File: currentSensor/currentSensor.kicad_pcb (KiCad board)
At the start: 2 copper layers, 60 x 100 mm, 54 parts, among them J1 Conn_01x09_Male, J2 Conn_01x09_Male, J3 Screw_Terminal_01x08, J4 Screw_Terminal_01x02, J5 Screw_Terminal_01x08, U1 PC847, U2 PC847, U3 PC847, U4 PC847

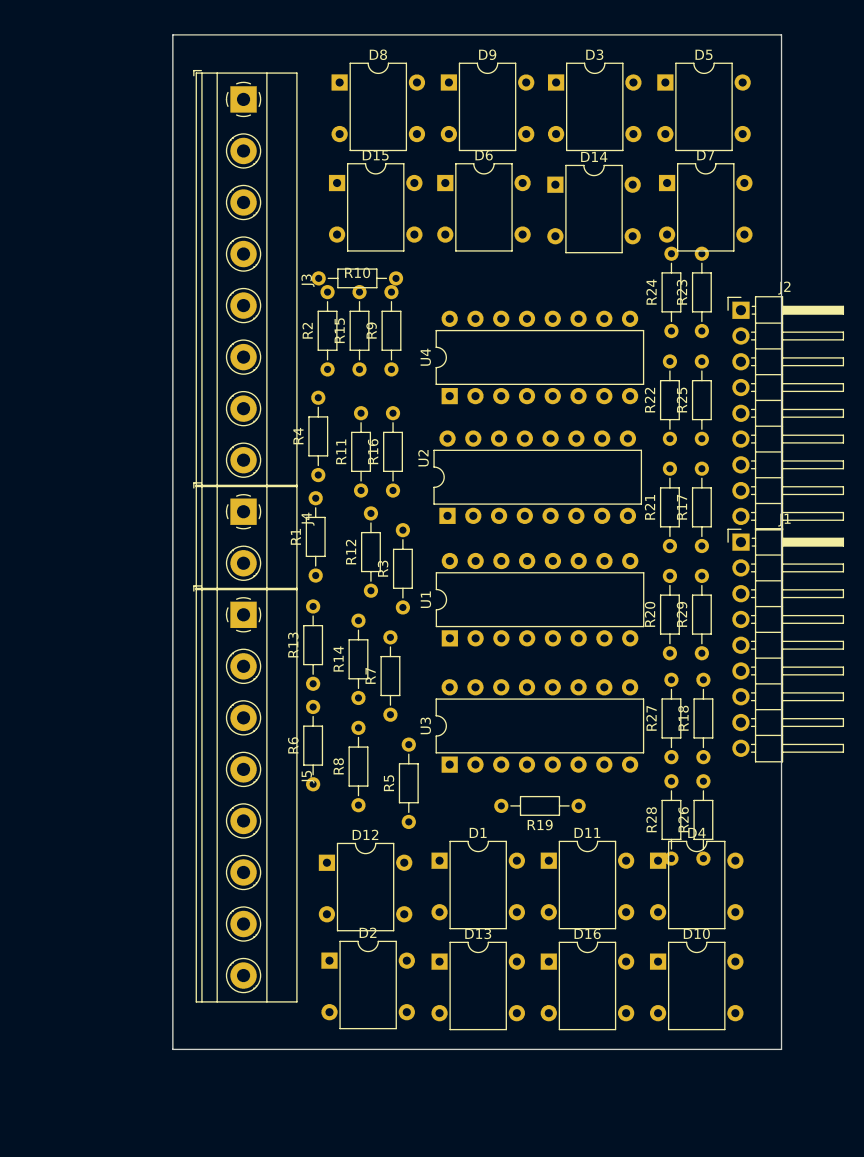
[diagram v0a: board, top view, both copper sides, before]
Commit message: added some changed to the current sensor. There also seems a bug with the mcp23017. I suspect the chip itself may be damaged. Not all pins are at 5V
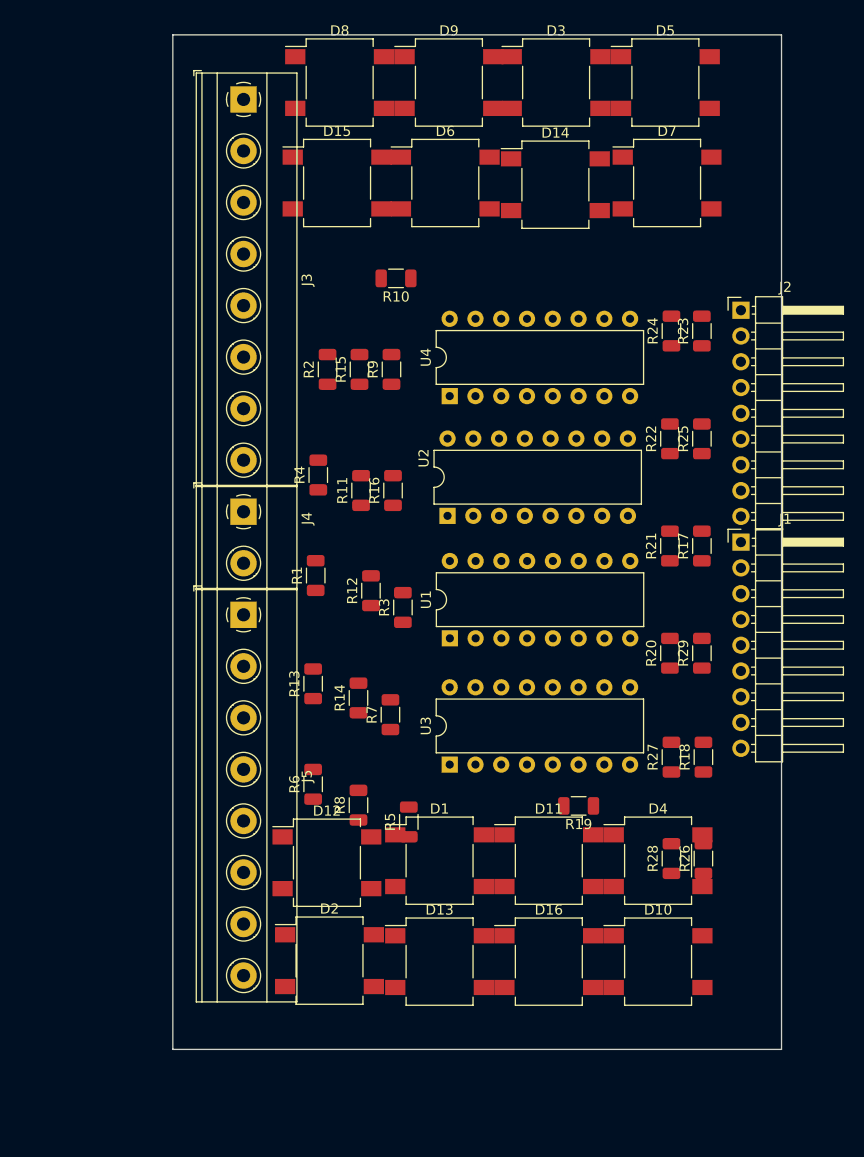
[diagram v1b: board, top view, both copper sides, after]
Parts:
- D1, D10, D11, D12, D13, D14, D15, D16, D2, D3, D4, D5, D6, D7, D8, D9: footprint Diode_THT:Diode_Bridge_DIP-4_W7.62mm_P5.08mm -> Diode_SMD:Diode_Bridge_Diotec_SO-DIL-Slim
- R1, R10, R11, R12, R13, R14, R15, R16, R17, R18, R19, R2, R20, R21, R22, R23, R24, R25, R26, R27, R28, R29, R3, R4, R5, R6, R7, R8, R9: footprint Resistor_THT:R_Axial_DIN0204_L3.6mm_D1.6mm_P7.62mm_Horizontal -> Resistor_SMD:R_1206_3216Metric

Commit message: added separate HAL files for NX and empty files for the MCP23017. They need filling in for read and write registers
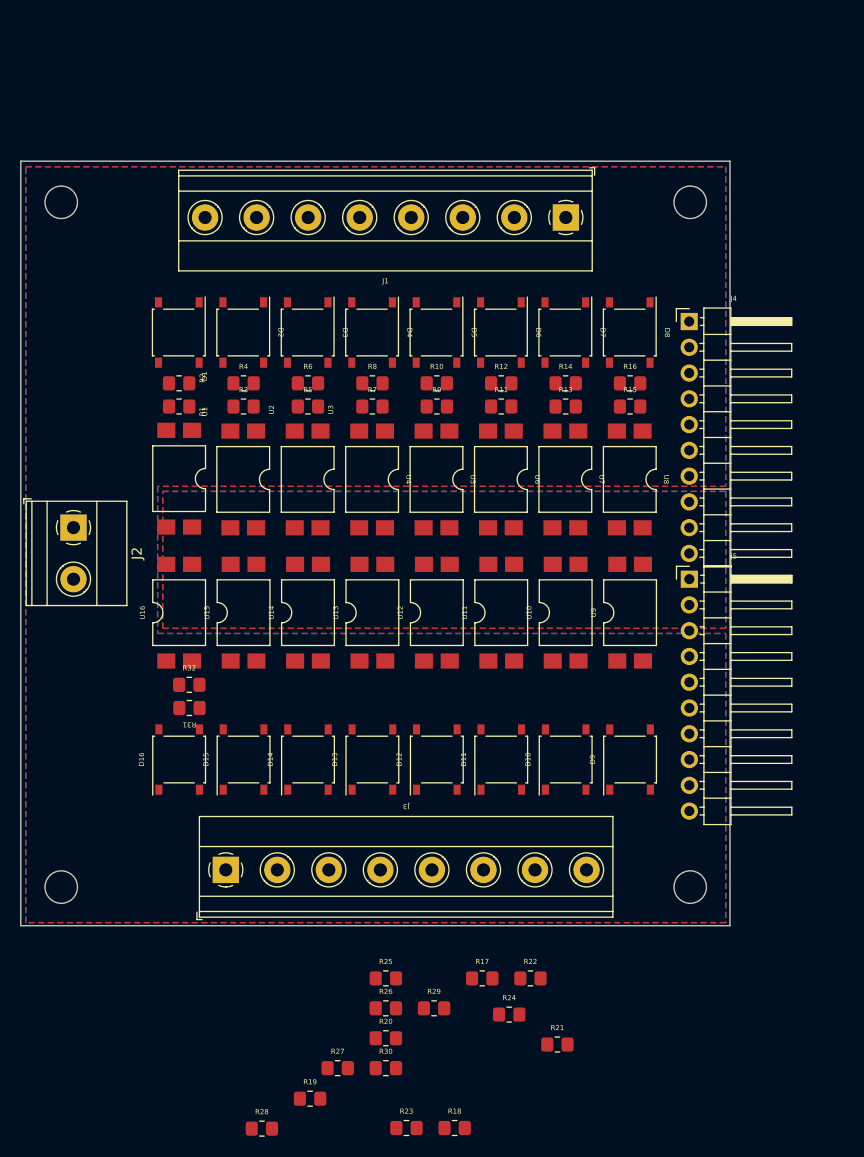
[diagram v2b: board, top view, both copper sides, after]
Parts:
- added R30: 4k7, Resistor_SMD:R_0805_2012Metric_Pad1.20x1.40mm_HandSolder, F.Cu at (44.0, 152.8)
- added R31: 47R, Resistor_SMD:R_0805_2012Metric_Pad1.20x1.40mm_HandSolder, F.Cu at (24.6, 117.3)
- added R32: 4k7, Resistor_SMD:R_0805_2012Metric_Pad1.20x1.40mm_HandSolder, F.Cu at (24.6, 115.1)
- added REF**: MountingHole_3.2mm_M3, MountingHole:MountingHole_3.2mm_M3, F.Cu at (74.0, 67.5)
- added REF**: MountingHole_3.2mm_M3, MountingHole:MountingHole_3.2mm_M3, F.Cu at (74.0, 135.0)
- added REF**: MountingHole_3.2mm_M3, MountingHole:MountingHole_3.2mm_M3, F.Cu at (12.0, 67.5)
- added REF**: MountingHole_3.2mm_M3, MountingHole:MountingHole_3.2mm_M3, F.Cu at (12.0, 135.0)
- added U10: SFH6206-2T, Package_DIP:SMDIP-4_W9.53mm_Clearance8mm, F.Cu at (61.7, 108.0)
- added U11: SFH6206-2T, Package_DIP:SMDIP-4_W9.53mm_Clearance8mm, F.Cu at (55.4, 108.0)
- added U12: SFH6206-2T, Package_DIP:SMDIP-4_W9.53mm_Clearance8mm, F.Cu at (49.0, 108.0)
- added U13: SFH6206-2T, Package_DIP:SMDIP-4_W9.53mm_Clearance8mm, F.Cu at (42.7, 108.0)
- added U14: SFH6206-2T, Package_DIP:SMDIP-4_W9.53mm_Clearance8mm, F.Cu at (36.3, 108.0)
- added U15: SFH6206-2T, Package_DIP:SMDIP-4_W9.53mm_Clearance8mm, F.Cu at (30.0, 108.0)
- added U16: SFH6206-2T, Package_DIP:SMDIP-4_W9.53mm_Clearance8mm, F.Cu at (23.6, 108.0)
- added U5: SFH6206-2T, Package_DIP:SMDIP-4_W9.53mm_Clearance8mm, F.Cu at (49.0, 94.8)
- added U6: SFH6206-2T, Package_DIP:SMDIP-4_W9.53mm_Clearance8mm, F.Cu at (55.3, 94.8)
- added U7: SFH6206-2T, Package_DIP:SMDIP-4_W9.53mm_Clearance8mm, F.Cu at (61.7, 94.8)
- added U8: SFH6206-2T, Package_DIP:SMDIP-4_W9.53mm_Clearance8mm, F.Cu at (68.0, 94.8)
- added U9: SFH6206-2T, Package_DIP:SMDIP-4_W9.53mm_Clearance8mm, F.Cu at (68.1, 108.0)
- D1, D10, D11, D12, D13, D14, D15, D16, D2, D3, D4, D5, D6, D7, D8, D9: value D -> ABS2; footprint Diode_SMD:Diode_Bridge_Diotec_SO-DIL-Slim -> Diode_SMD:Diode_Bridge_Diotec_ABS
- J1: value Conn_01x09_Male -> Screw_Terminal_01x08; footprint Connector_PinHeader_2.54mm:PinHeader_1x09_P2.54mm_Horizontal -> TerminalBlock_Phoenix:TerminalBlock_Phoenix_MKDS-1,5-8-5.08_1x08_P5.08mm_Horizontal
- J2: value Conn_01x09_Male -> Screw_Terminal_01x02; footprint Connector_PinHeader_2.54mm:PinHeader_1x09_P2.54mm_Horizontal -> TerminalBlock_Phoenix:TerminalBlock_Phoenix_MKDS-1,5-2-5.08_1x02_P5.08mm_Horizontal
- J4: value Screw_Terminal_01x02 -> Conn_01x10_Male; footprint TerminalBlock_Phoenix:TerminalBlock_Phoenix_MKDS-1,5-2-5.08_1x02_P5.08mm_Horizontal -> Connector_PinHeader_2.54mm:PinHeader_1x10_P2.54mm_Horizontal
- J5: value Screw_Terminal_01x08 -> Conn_01x10_Male; footprint TerminalBlock_Phoenix:TerminalBlock_Phoenix_MKDS-1,5-8-5.08_1x08_P5.08mm_Horizontal -> Connector_PinHeader_2.54mm:PinHeader_1x10_P2.54mm_Horizontal
- R1, R11, R13, R15, R17, R19, R21, R23, R25, R27, R29, R3, R5, R7, R9: value R -> 47R; footprint Resistor_SMD:R_1206_3216Metric -> Resistor_SMD:R_0805_2012Metric_Pad1.20x1.40mm_HandSolder
- R10, R12, R14, R16, R18, R2, R20, R22, R24, R26, R28, R4, R6, R8: value R -> 4k7; footprint Resistor_SMD:R_1206_3216Metric -> Resistor_SMD:R_0805_2012Metric_Pad1.20x1.40mm_HandSolder
- U1, U2, U3, U4: value PC847 -> SFH6206-2T; footprint Package_DIP:DIP-16_W7.62mm -> Package_DIP:SMDIP-4_W9.53mm_Clearance8mm
- moved R23 83.8 mm to (46.0, 158.8), turned to 0 degrees
- moved J3 76.0 mm to (28.2, 133.3), turned to 0 degrees
- moved R24 69.2 mm to (56.2, 147.6), turned to 0 degrees
- moved J2 69.2 mm to (13.2, 99.6), turned to -90 degrees
- moved D9 69.1 mm to (68.1, 122.4), turned to 90 degrees
- moved D2 62.5 mm to (29.9, 80.3), turned to -90 degrees
- moved D14 61.7 mm to (36.3, 122.4), turned to 90 degrees
- moved R25 61.6 mm to (44.0, 144.0), turned to 0 degrees
- moved D4 59.2 mm to (42.6, 80.3), turned to -90 degrees
- moved D1 58.1 mm to (23.6, 80.3), turned to -90 degrees
- moved D15 57.6 mm to (30.0, 122.4), turned to 90 degrees
- moved R22 54.9 mm to (58.2, 144.0), turned to 0 degrees
- moved R21 50.4 mm to (60.9, 150.5), turned to 0 degrees
- moved R28 48.4 mm to (31.8, 158.8), turned to 0 degrees
- moved R17 47.8 mm to (53.5, 144.0), turned to 0 degrees
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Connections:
- D1 pad 3: track5 -> track1
- D2 pad 3: track6 -> track2
- D3 pad 3: track7 -> track3
- D4 pad 3: track8 -> track4
- D5 pad 3: track1 -> track5
- D6 pad 3: track2 -> track6
- D7 pad 3: track3 -> track7
- D8 pad 3: track4 -> track8
- J1 pad 1: GND -> track8
- J1 pad 2: inp8 -> track7
- J1 pad 3: inp7 -> track6
- J1 pad 4: inp6 -> track5
- J1 pad 5: inp5 -> track4
- J1 pad 6: inp4 -> track3
- J1 pad 7: inp3 -> track2
- J1 pad 8: inp2 -> track1
- J2 pad 1: inp16 -> COM
- J2 pad 2: inp15 -> COM
- J3 pad 1: track1 -> track16
- J3 pad 2: track2 -> track15
- J3 pad 3: track3 -> track14
- J3 pad 4: track4 -> track13
- J3 pad 5: track5 -> track12
- J3 pad 6: track6 -> track11
- J3 pad 7: track7 -> track10
- J3 pad 8: track8 -> track9
- J4 pad 1: COM -> +5V
- J4 pad 2: COM -> inp1
- J5 pad 1: track9 -> +5V
- J5 pad 2: track10 -> inp9
- J5 pad 3: track11 -> inp10
- J5 pad 4: track12 -> inp11
- J5 pad 5: track13 -> inp12
- J5 pad 6: track14 -> inp13
- J5 pad 7: track15 -> inp14
- J5 pad 8: track16 -> inp15
- R1 pad 1: track5 -> track1
- R10 pad 1: track10 -> track5
- R10 pad 2: Net-(R10-Pad2) -> COM
- R11 pad 1: track11 -> track6
- R12 pad 1: track12 -> track6
- R12 pad 2: Net-(R12-Pad2) -> COM
- R13 pad 1: track13 -> track7
- R14 pad 1: track14 -> track7
- R14 pad 2: Net-(R14-Pad2) -> COM
- R15 pad 1: track15 -> track8
- R16 pad 1: track16 -> track8
- R16 pad 2: Net-(R16-Pad2) -> COM
- R17 pad 1: track5 -> track9
- R17 pad 2: COM -> Net-(R17-Pad2)
- R18 pad 1: track6 -> track9
- R19 pad 1: track7 -> track10
- R19 pad 2: COM -> Net-(R19-Pad2)
- R2 pad 1: track6 -> track1
- R2 pad 2: Net-(R2-Pad2) -> COM
- R20 pad 1: track8 -> track10
- R21 pad 1: track1 -> track11
- R21 pad 2: COM -> Net-(R21-Pad2)
- R22 pad 1: track2 -> track11
- R23 pad 1: track3 -> track12
- R23 pad 2: COM -> Net-(R23-Pad2)
- R24 pad 1: track4 -> track12
- R25 pad 1: track9 -> track13
- R25 pad 2: COM -> Net-(R25-Pad2)
- R26 pad 1: track10 -> track13
- R27 pad 1: track11 -> track14
- R27 pad 2: COM -> Net-(R27-Pad2)
- R28 pad 1: track12 -> track14
- R29 pad 1: track13 -> track15
- R29 pad 2: COM -> Net-(R29-Pad2)
- R3 pad 1: track7 -> track2
- R4 pad 1: track8 -> track2
- R4 pad 2: Net-(R4-Pad2) -> COM
- R5 pad 1: track1 -> track3
- R6 pad 1: track2 -> track3
- R6 pad 2: Net-(R6-Pad2) -> COM
- R7 pad 1: track3 -> track4
- R8 pad 2: Net-(R8-Pad2) -> COM
- R9 pad 1: track9 -> track5
- U1 pad 3: Net-(R2-Pad2) -> GND
- U1 pad 4: COM -> inp1
- U2 pad 1: Net-(R5-Pad2) -> Net-(R3-Pad2)
- U2 pad 3: Net-(R6-Pad2) -> GND
- U2 pad 4: COM -> inp2
- U3 pad 1: Net-(R9-Pad2) -> Net-(R5-Pad2)
- U3 pad 3: Net-(R10-Pad2) -> GND
- U3 pad 4: COM -> inp3
- U4 pad 1: Net-(R13-Pad2) -> Net-(R7-Pad2)
- U4 pad 3: Net-(R14-Pad2) -> GND
- U4 pad 4: COM -> inp4
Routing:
- added copper zone on B.Cu, net COM
- added copper zone on F.Cu, net COM
- added copper zone on B.Cu, net GND
- added copper zone on F.Cu, net GND
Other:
- board size 60 x 100 mm -> 69.9 x 75.4 mm
